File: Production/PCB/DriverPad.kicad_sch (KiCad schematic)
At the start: 37 parts, among them SW1 SW_Push, SW2 SW_Push, SW3 SW_Push, SW4 SW_Push, SW5 SW_Push, SW6 SW_Push, SW7 SW_Push, SW8 SW_Push, U1 MOUDLE-SEEEDUINO-XIAO, U2 ER_OLEDM0.91_1x-I2C, U3 74AHCT125

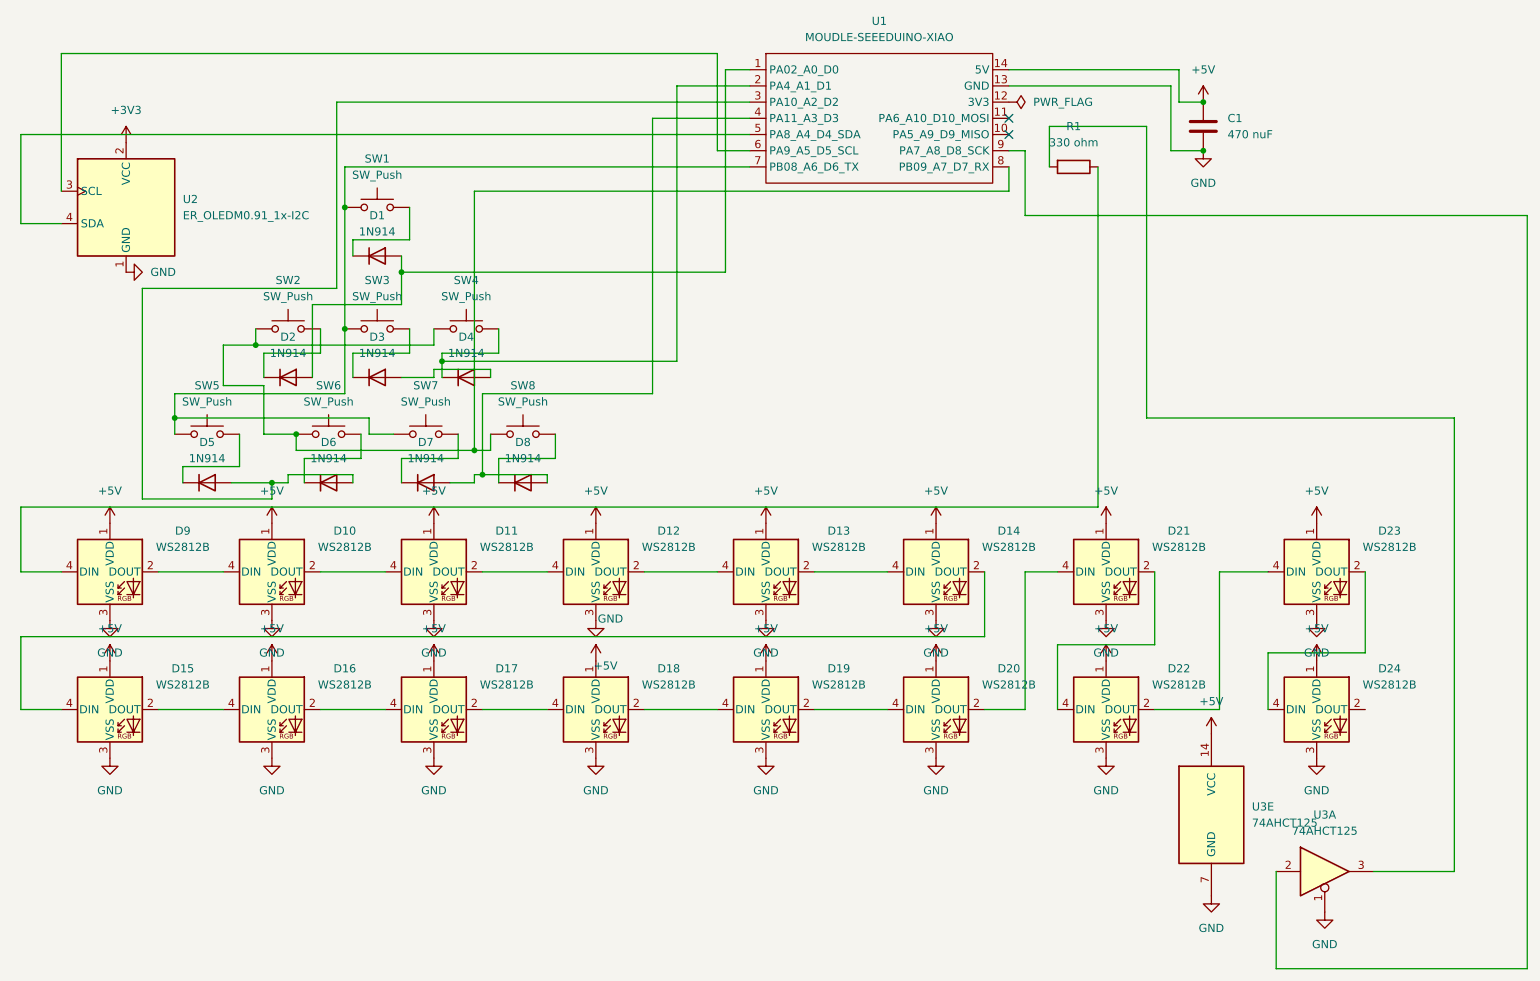
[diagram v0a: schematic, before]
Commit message: finished kicad tracing and exported gerbers
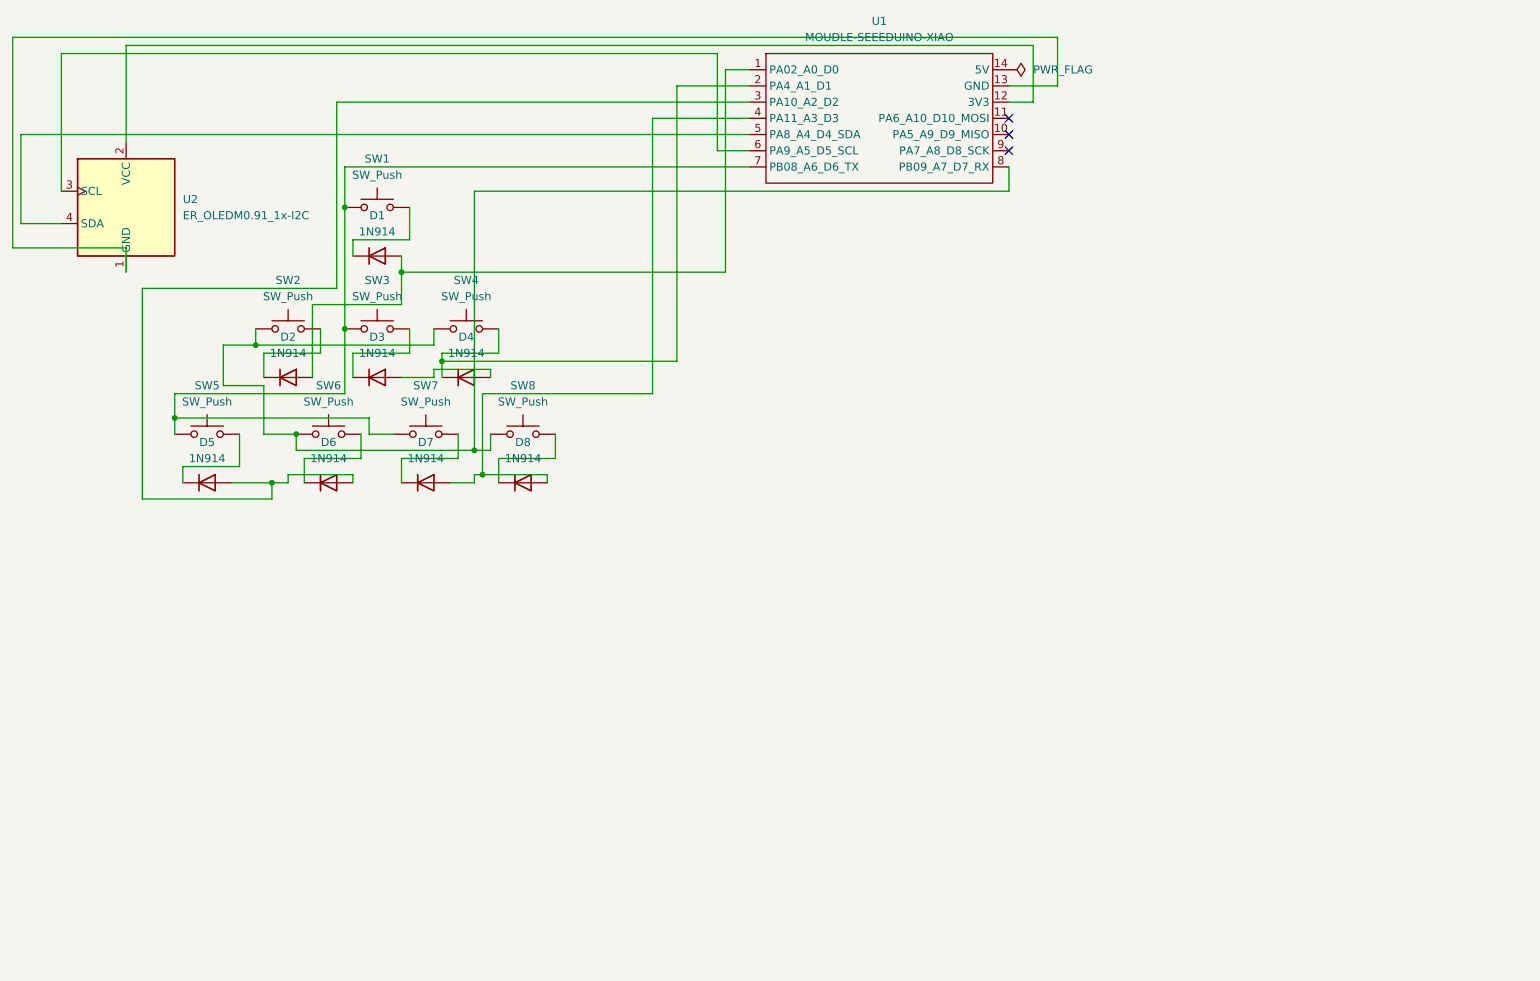
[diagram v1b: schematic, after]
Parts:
- removed C1: 470 nuF, symbol Device:C
- removed D10, D11, D12, D13, D14, D15, D16, D17, D18, D19, D20, D21, D22, D23, D24, D9: WS2812B, LED_SMD:LED_WS2812B_PLCC4_5.0x5.0mm_P3.2mm, symbol LED:WS2812B
- removed R1: 330 ohm, Resistor_THT:R_Axial_DIN0207_L6.3mm_D2.5mm_P10.16mm_Horizontal, symbol Device:R
- removed U3: 74AHCT125, Package_DIP:DIP-14_W7.62mm, symbol 74xx:74AHCT125
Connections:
- net +3V3 is gone; now on an unnamed net: U2.2 (VCC)
- net +5V: no longer names the net of U1.14 (5V)
- net GND: no longer names the net of U1.13 (GND), U2.1 (GND)
- no-connect marks 2 -> 3
